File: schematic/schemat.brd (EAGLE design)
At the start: 94.9 x 88 mm, 73 parts, among them IC1 TB6612FNG, IC2 LM339D, IC3 7806DT, Q1 16MHz

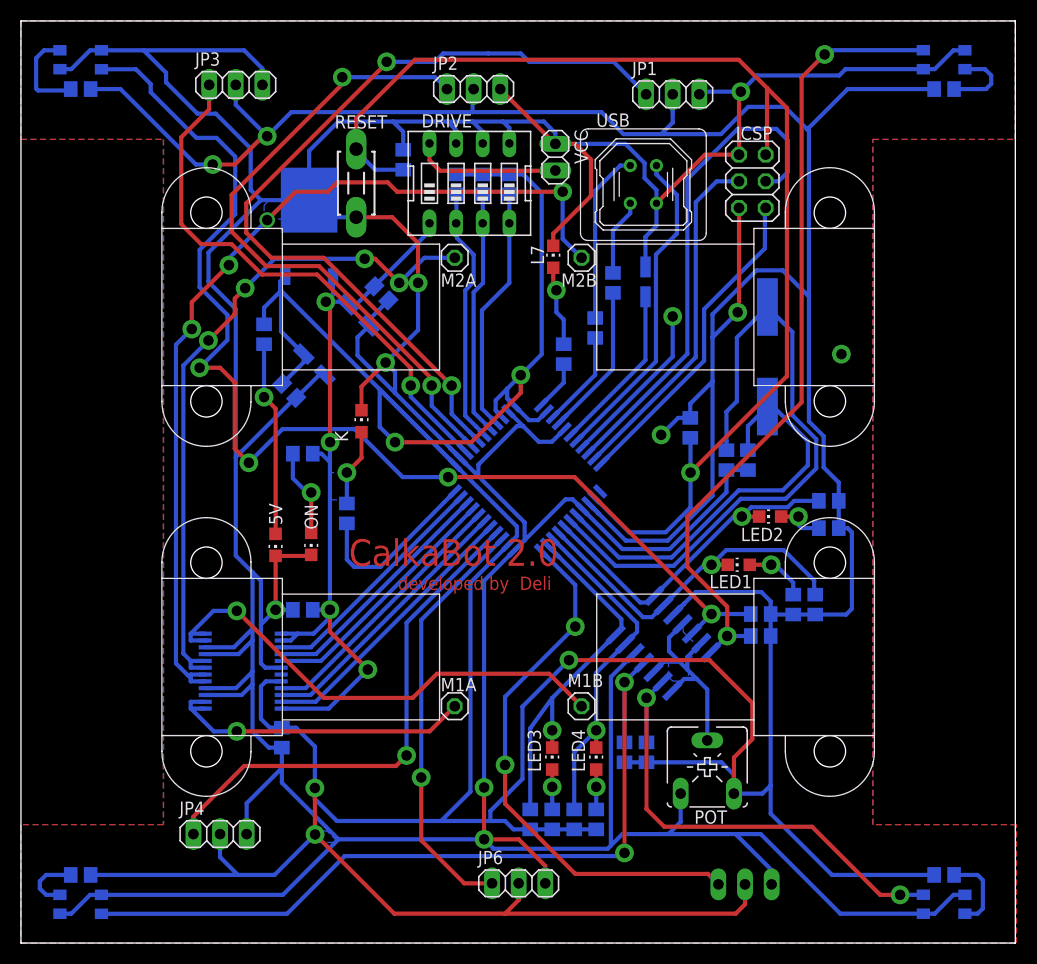
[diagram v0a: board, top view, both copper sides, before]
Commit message: zmiana viasow na 0.5/1.3
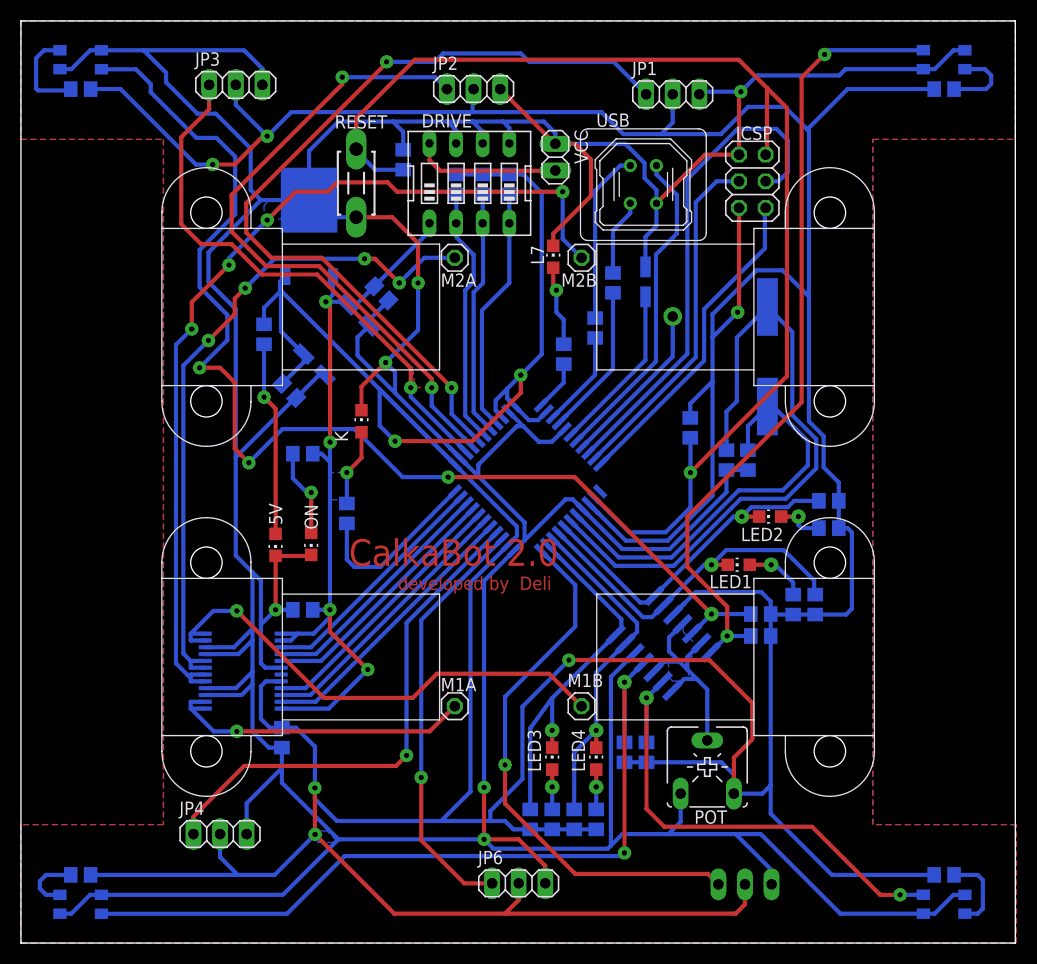
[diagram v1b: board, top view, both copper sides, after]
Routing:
- net VCC: track 618.1 -> 613.5 mm, vias 9 -> 8
- net I/O8: vias 2 -> 1
- added copper zone on layer 1, net N$24
